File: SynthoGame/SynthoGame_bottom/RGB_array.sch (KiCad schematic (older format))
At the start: 41 parts, among them J5 FH12-6S-0.5SH_55_

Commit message: Moving to right directories
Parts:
- J5: symbol EnvOpenPico-rescue:FH12-6S-0.5SH_55_-FH12-6S-0.5SH_55_ -> SynthoGame-rescue:FH12-6S-0.5SH_55_-FH12-6S-0.5SH_55_
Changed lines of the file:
@@
 5V
 $Comp
-L EnvOpenPico-rescue:FH12-6S-0.5SH_55_-FH12-6S-0.5SH_55_ J5
+L SynthoGame-rescue:FH12-6S-0.5SH_55_-FH12-6S-0.5SH_55_ J5
 U 1 1 6249AFDD
 P 1900 3700

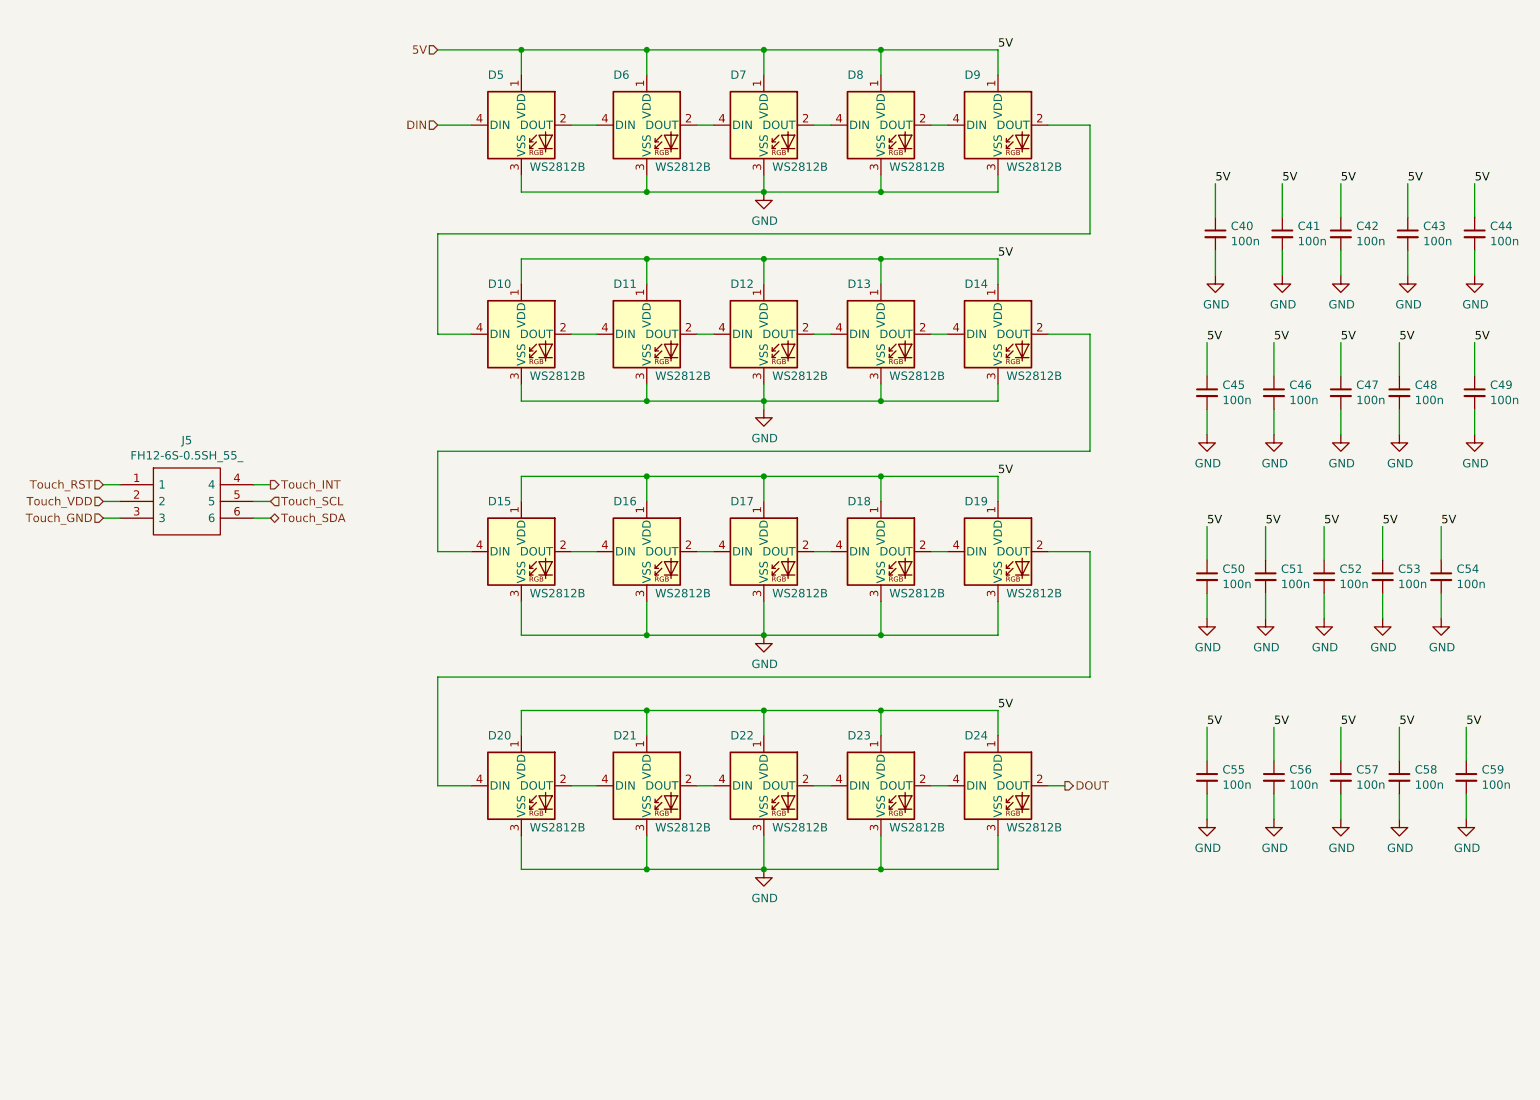
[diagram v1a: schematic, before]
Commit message: add board shape, main component placement
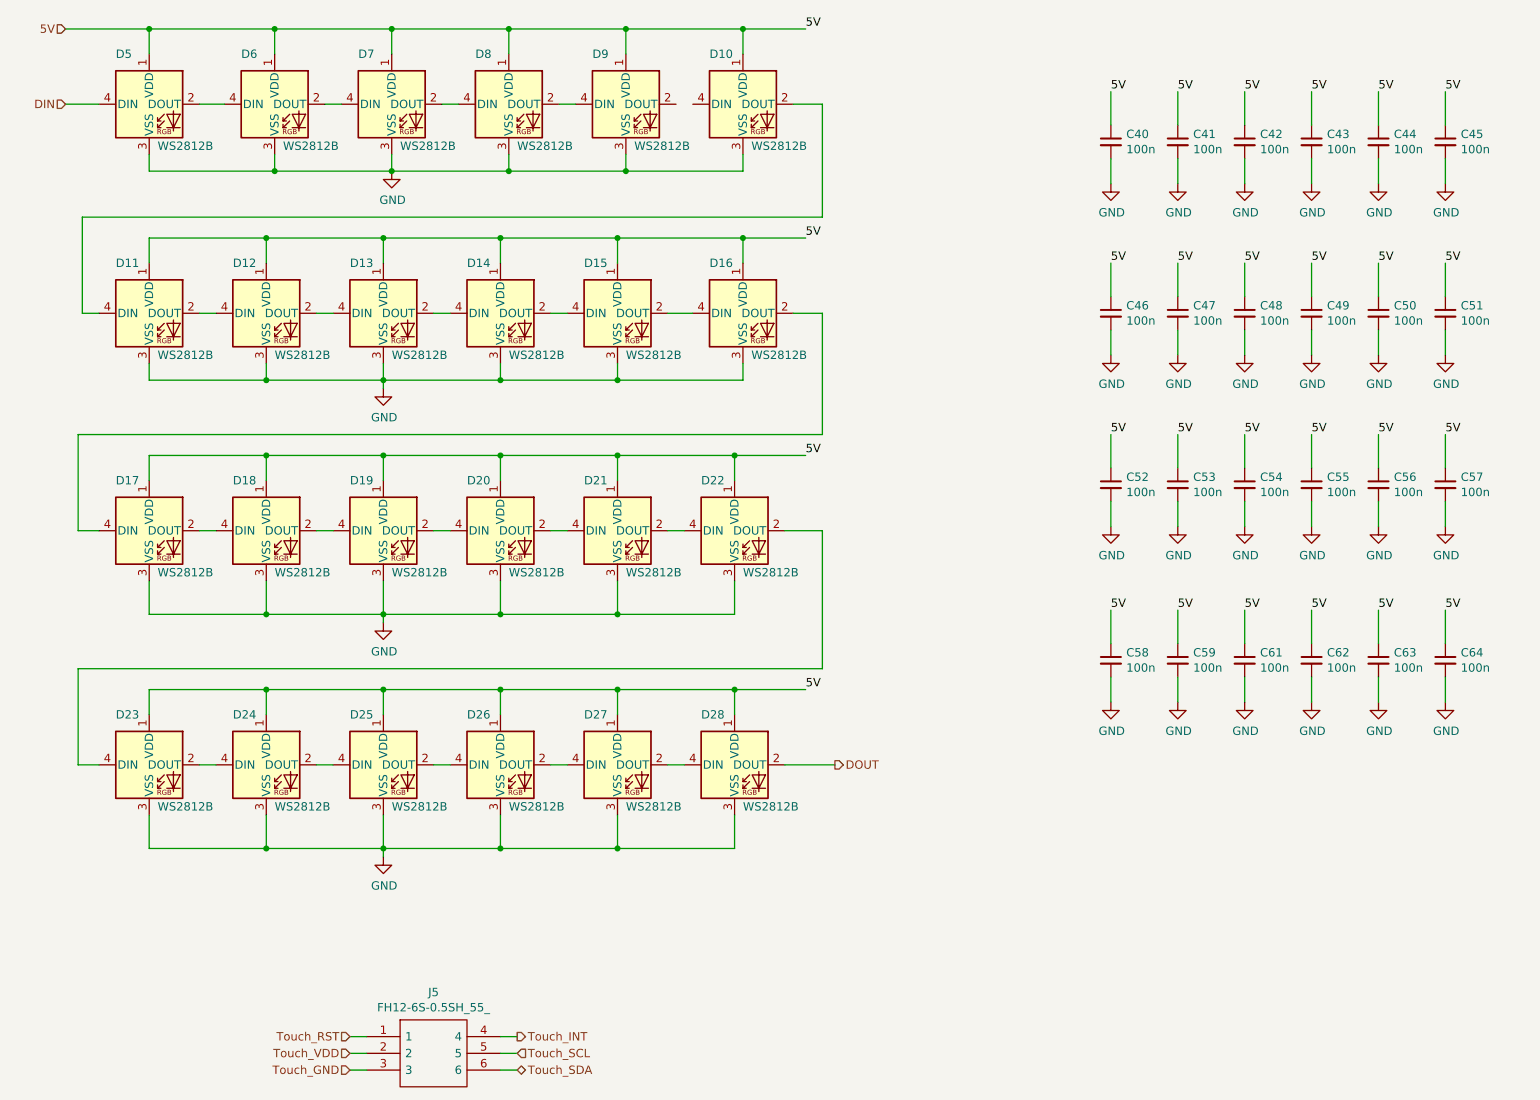
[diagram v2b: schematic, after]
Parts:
- added C61, C62, C63, C64: 100n, Capacitor_SMD:C_0402_1005Metric, symbol Device:C_Small
- added D25, D26, D27, D28: WS2812B, LED_SMD:LED_WS2812B_PLCC4_5.0x5.0mm_P3.2mm, symbol LED:WS2812B
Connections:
- net 5V: now also C61.1, C62.1, C63.1, C64.1, D25.1 (VDD), D26.1 (VDD), D27.1 (VDD), D28.1 (VDD)
- net DOUT: now also D28.2 (DOUT); no longer D24.2 (DOUT)
- net GND: now also C61.2, C62.2, C63.2, C64.2, D25.3 (VSS), D26.3 (VSS), D27.3 (VSS), D28.3 (VSS)
- net at D9.2 (DOUT): no longer D10.4 (DIN)
- new net: D25.2 (DOUT), D26.4 (DIN)
- new net: D24.2 (DOUT), D25.4 (DIN)
- new net: D26.2 (DOUT), D27.4 (DIN)
- new net: D27.2 (DOUT), D28.4 (DIN)
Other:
- moved on the sheet: C40, C41, C42, C43, C44, C45, C46, C47, C48, C49, C50, C51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

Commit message: resolve ERC errors, minor tweaks
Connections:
- net at D9.2 (DOUT): now also D10.4 (DIN)
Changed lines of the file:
@@
 Wire Wire Line
 	1650 5375 1775 5375
+Wire Wire Line
+	5225 1425 5325 1425
 $EndSCHEMATC
